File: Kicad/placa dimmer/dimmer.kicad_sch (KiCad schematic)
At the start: 52 parts, among them J1 Screw_Terminal_01x02, J2 Screw_Terminal_01x02, J3 Screw_Terminal_01x02, J4 Conn_01x05_Socket, Q1 2N7000, Q2 2N7000, U1 MOC3023M, U2 4N25, U3 74HC14, U4 MOC3023M

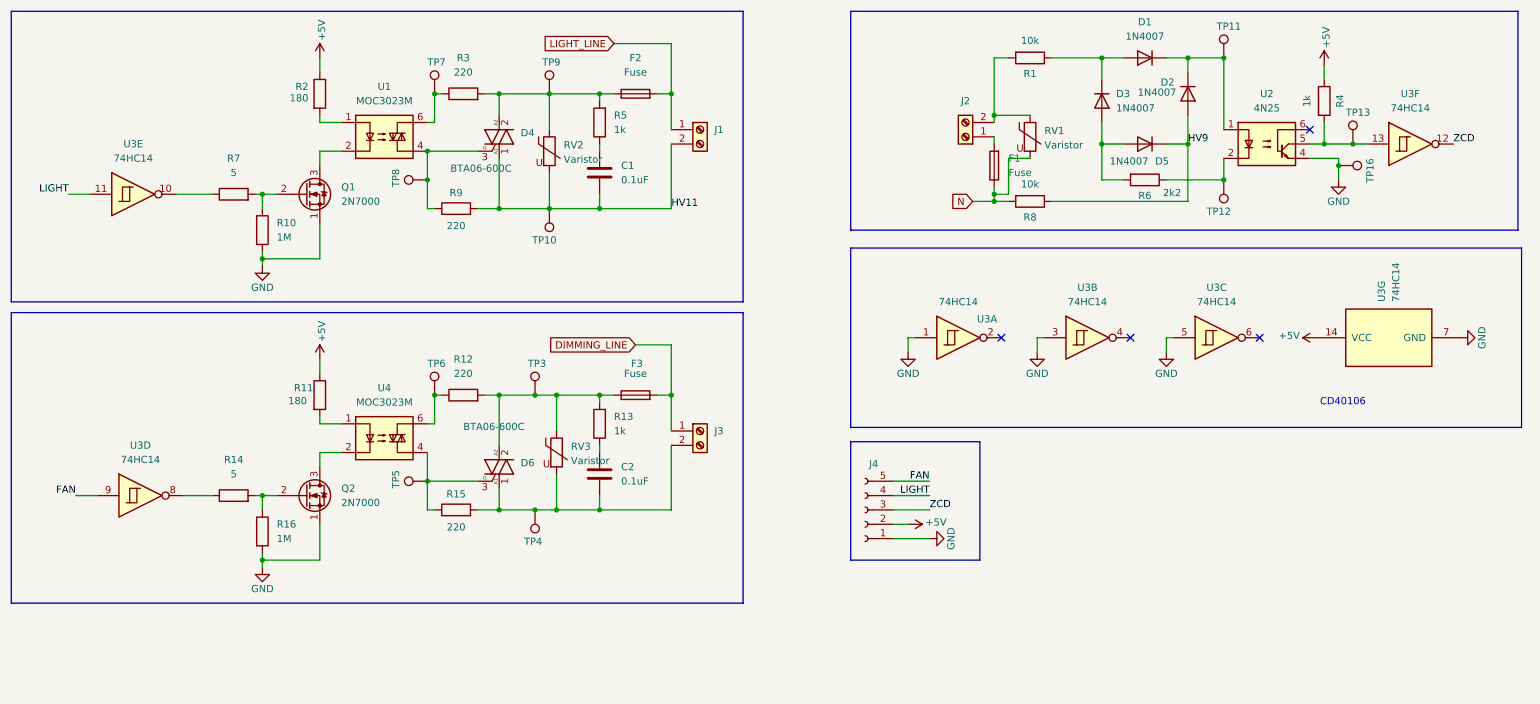
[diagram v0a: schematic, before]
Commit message: arreglos
arreglos comentados en el pull request
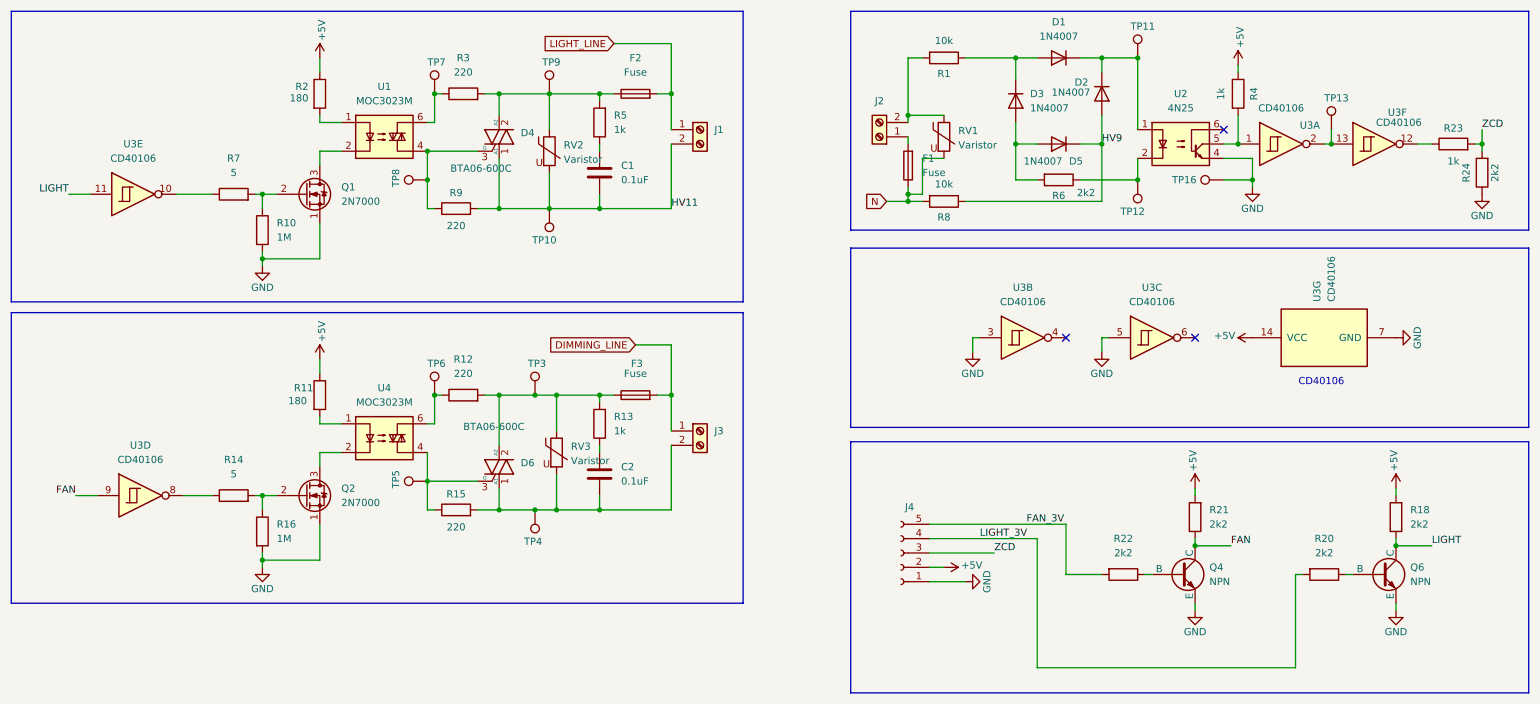
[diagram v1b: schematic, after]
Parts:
- added Q4, Q6: NPN, Package_TO_SOT_THT:TO-92_Wide, symbol Simulation_SPICE:NPN
- added R18, R20, R21, R22, R24: 2k2, Resistor_THT:R_Axial_DIN0207_L6.3mm_D2.5mm_P7.62mm_Horizontal, symbol Device:R
- added R23: 1k, Resistor_THT:R_Axial_DIN0207_L6.3mm_D2.5mm_P10.16mm_Horizontal, symbol Device:R
- U3: value 74HC14 -> CD40106
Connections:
- net +5V: now also R18.2, R21.2
- net FAN: now also Q4.1 (C), R21.1; no longer J4.5 (Pin_5)
- net GND: now also Q4.3 (E), Q6.3 (E), R24.1; no longer U3.1
- net LIGHT: now also Q6.1 (C), R18.1; no longer J4.4 (Pin_4)
- net ZCD: now also R23.2, R24.2; no longer U3.12
- net at U3.2: now also TP13.1, U3.13
- net at R4.2, U2.5: now also U3.1; no longer TP13.1, U3.13
- new net: Q4.2 (B), R22.1
- new net: R23.1, U3.12
- new net: Q6.2 (B), R20.1
- new net FAN_3V: J4.5 (Pin_5), R22.2
- new net LIGHT_3V: J4.4 (Pin_4), R20.2
- no-connect marks 4 -> 3
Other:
- moved on the sheet: D1, D2, D3, D5, F1, J2, J4, R1, R4, R6, R8, RV1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
